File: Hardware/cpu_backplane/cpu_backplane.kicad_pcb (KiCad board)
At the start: 2 copper layers, 149.9 x 99.9 mm, 93 parts, among them J1 USB_B_Micro, J2 Conn_02x02_Odd_Even, J3 Conn_01x06, SW1 SW_SPST, U1 74AC161, U2 MAX811SEUS-T, U3 MAX811SEUS-T, U4 PAL24, U5 GAL16V8, U6 W65C02SxP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

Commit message: Fix missing signals
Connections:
- U5 pad 14: Net-(U5-Pad14) -> ~SIRQ~
- U9 pad 26: Net-(U9-Pad26) -> ~SIRQ~
- U9 pad 27: Net-(U9-Pad27) -> CLK
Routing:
- net ~SIRQ~: track 0.00 -> 63.2 mm, vias 0 -> 3
- net CLK: track 227.7 -> 268.8 mm, vias 7 -> 8
- net R~W~: track 268.9 -> 272.9 mm
- net /~DSR~: track 40.0 -> 44.0 mm

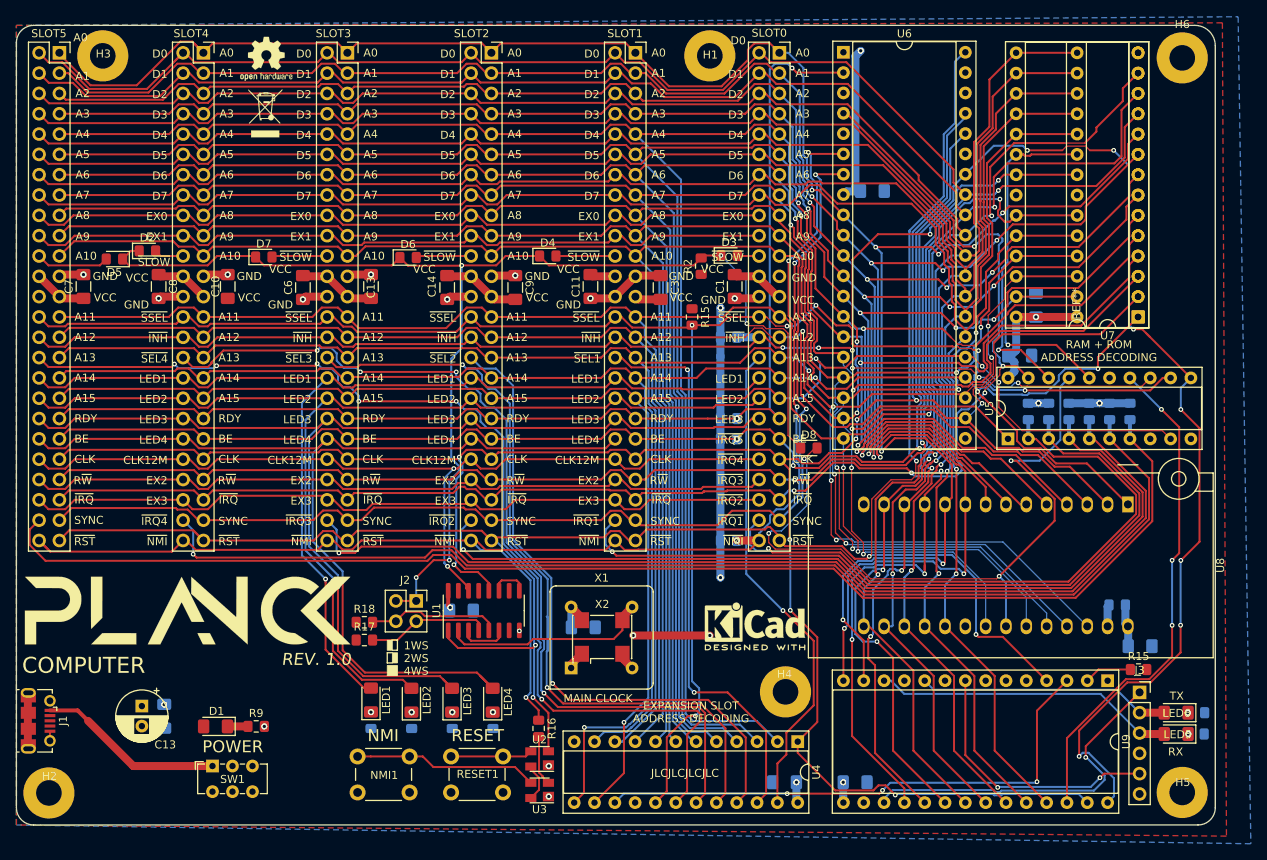
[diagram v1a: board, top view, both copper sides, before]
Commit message: Finishing CPU backplane with through hole components
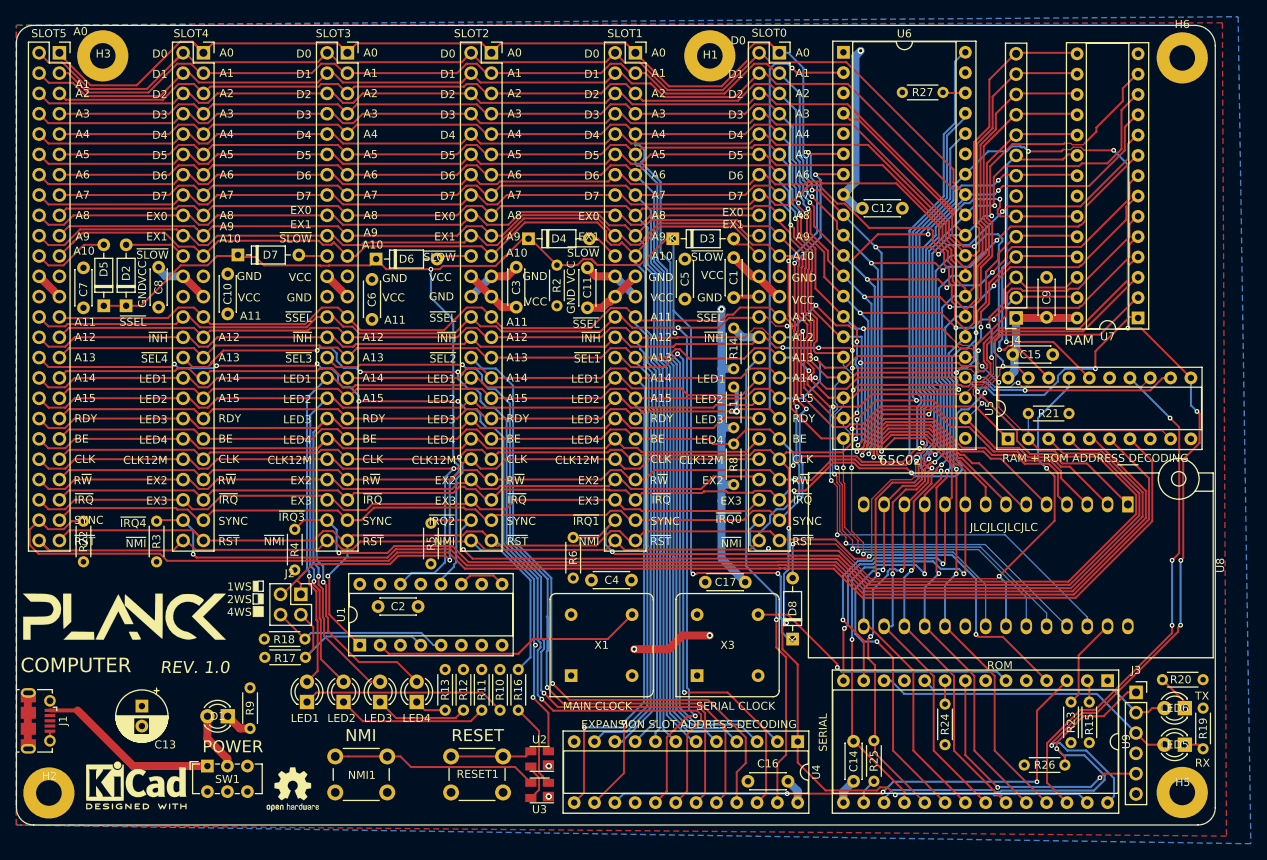
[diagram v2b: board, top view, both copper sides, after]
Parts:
- removed the C13 at (44.3, 32.6)
- removed the C14 at (53.8, 32.8)
- removed the C5 at (140.5, 77.6)
- removed the C5 at (55.6, 73.2)
- removed the C9 at (62.4, 32.8)
- removed the G*** at (21.4, 73.2)
- removed the G*** at (21.6, 73.7)
- removed H4: MountingHole_Pad, MountingHole:MountingHole_3.2mm_M3_Pad
- removed the R15 at (140.3, 80.5)
- removed the R15 at (84.5, 36.4)
- removed R7: 1k, Resistor_SMD:R_0805_2012Metric_Pad1.15x1.40mm_HandSolder
- removed the REF** at (140.2, 36.4)
- removed the REF** at (31.1, 11.0)
- removed X2: SG-7050CAN, Oscillator:Oscillator_SMD_SeikoEpson_SG8002CA-4Pin_7.0x5.0mm
- added C17: 10n, Capacitor_THT:C_Disc_D4.3mm_W1.9mm_P5.00mm, F.Cu at (86.1, 69.6)
- added C5: 10n, Capacitor_THT:C_Disc_D4.3mm_W1.9mm_P5.00mm, F.Cu at (83.6, 29.2)
- added G***: LOGO, Logo:logo-sm, B.Cu at (14.7, 74.4)
- added G***: LOGO, Logo:logo-sm, F.Cu at (13.5, 73.9)
- added J4: Conn_01x14, Connector_PinSocket_2.54mm:PinSocket_1x14_P2.54mm_Vertical, F.Cu at (125.0, 36.6)
- added R15: 10k, Resistor_THT:R_Axial_DIN0204_L3.6mm_D1.6mm_P5.08mm_Horizontal, F.Cu at (134.1, 84.6)
- added R24: 10k, Resistor_THT:R_Axial_DIN0204_L3.6mm_D1.6mm_P5.08mm_Horizontal, F.Cu at (116.1, 89.9)
- added R25: 10k, Resistor_THT:R_Axial_DIN0204_L3.6mm_D1.6mm_P5.08mm_Horizontal, F.Cu at (107.2, 89.4)
- added R26: 10k, Resistor_THT:R_Axial_DIN0204_L3.6mm_D1.6mm_P5.08mm_Horizontal, F.Cu at (126.0, 92.5)
- added R27: 10k, Resistor_THT:R_Axial_DIN0204_L3.6mm_D1.6mm_P5.08mm_Horizontal, F.Cu at (110.7, 8.38)
- added X3: 1.8432MHz, Oscillator:Oscillator_DIP-8, F.Cu at (85.1, 81.3)
- C1, C10, C11, C3, C6, C7, C8: footprint Capacitor_SMD:C_1206_3216Metric_Pad1.42x1.75mm_HandSolder -> Capacitor_THT:C_Disc_D4.3mm_W1.9mm_P5.00mm
- C12, C14, C15, C16, C2, C4, C9: footprint Capacitor_SMD:C_1206_3216Metric_Pad1.42x1.75mm_HandSolder -> Capacitor_THT:C_Disc_D4.3mm_W1.9mm_P5.00mm; moved to F.Cu
- D1, LED1, LED2, LED3, LED4, LED5, LED6: footprint LED_SMD:LED_1206_3216Metric_Pad1.42x1.75mm_HandSolder -> LED_THT:LED_D3.0mm
- D2, D3, D4, D5, D6, D7, D8: footprint Diode_SMD:D_0805_2012Metric_Pad1.15x1.40mm_HandSolder -> Diode_THT:D_DO-35_SOD27_P7.62mm_Horizontal
- R1, R10, R11, R12, R13, R14, R19, R20, R21, R22, R23, R3, R4, R5, R6, R8: footprint Resistor_SMD:R_0805_2012Metric_Pad1.15x1.40mm_HandSolder -> Resistor_THT:R_Axial_DIN0204_L3.6mm_D1.6mm_P5.08mm_Horizontal; moved to F.Cu
- R16, R17, R18, R2, R9: footprint Resistor_SMD:R_0805_2012Metric_Pad1.15x1.40mm_HandSolder -> Resistor_THT:R_Axial_DIN0204_L3.6mm_D1.6mm_P5.08mm_Horizontal
- U1: footprint Package_SO:SOIC-16_3.9x9.9mm_P1.27mm -> Package_DIP:DIP-16_W7.62mm_Socket
- moved R22 132.2 mm to (8.38, 67.1), turned to 90 degrees
- moved R3 120.6 mm to (17.5, 67.1), turned to 90 degrees
- moved R4 101.3 mm to (34.8, 68.1), turned to 90 degrees
- moved REF** 91.4 mm to (34.5, 95.5)
- moved R5 82.0 mm to (51.8, 67.3), turned to 90 degrees
- moved REF** 79.9 mm to (15.0, 95.0)
- moved R6 63.0 mm to (69.6, 69.1), turned to 90 degrees
- moved C2 30.0 mm to (45.2, 72.6), turned to 0 degrees
- moved D8 24.0 mm to (97.0, 76.7), turned to 90 degrees
- moved R2 18.7 mm to (67.6, 35.1)
- moved C3 18.2 mm to (62.5, 30.2)
- moved R23 18.2 mm to (131.8, 89.7), turned to 90 degrees
- moved R10 16.2 mm to (60.5, 85.6), turned to 90 degrees
- moved U1 16.1 mm to (42.9, 77.5)
- moved J2 14.4 mm to (35.6, 71.1)
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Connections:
- SLOT0 pad 40: LDE4 -> LED4
- U9 pad 16: GND -> Net-(R25-Pad2)
- U9 pad 9: GND -> /~CTS~
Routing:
- net ~SLOW~: track 160.1 -> 211.4 mm
- net Net-(U9-Pad6): track 0.00 -> 34.7 mm, vias 0 -> 1
- net Net-(LED1-Pad1): track 0.00 -> 25.5 mm, vias 1 -> 0
- net +5V: track 157.7 -> 134.5 mm, vias 10 -> 2
- net ~ROM_CS~: track 88.5 -> 69.2 mm, vias 4 -> 3
- net Net-(LED2-Pad1): track 0.00 -> 18.8 mm, vias 1 -> 0
- net GND: track 54.5 -> 37.4 mm, vias 16 -> 4
- net Net-(LED3-Pad1): track 0.00 -> 11.6 mm, vias 1 -> 0
- net LED3: track 144.1 -> 132.8 mm
- net ~NMI~: track 185.6 -> 176.1 mm, vias 5 -> 3
- net /~DSR~: track 44.0 -> 53.3 mm
- net Net-(R23-Pad2): track 2.74 -> 11.4 mm
- net LED2: track 141.2 -> 132.9 mm
- net /CLK_24M: track 25.9 -> 34.0 mm
- net A10: track 279.8 -> 286.8 mm
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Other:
- rule pad_to_mask_clearance: 0.05 -> 0
- board text added: "65C02"
- board text added: "RAM"
- board text added: "ROM"
- board text added: "SERIAL"
- board text added: "SERIAL CLOCK"
- board text added: "https://planck6502.com"
- board text added: "~IRQ0~"
- board text added: "©Jonathan Foucher 2021"
- board text removed: "~IRQ5~"

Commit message: update schematic and gerbers
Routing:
- net A8: track 283.5 -> 284.5 mm
- net ~RESET~: track 257.5 -> 258.1 mm

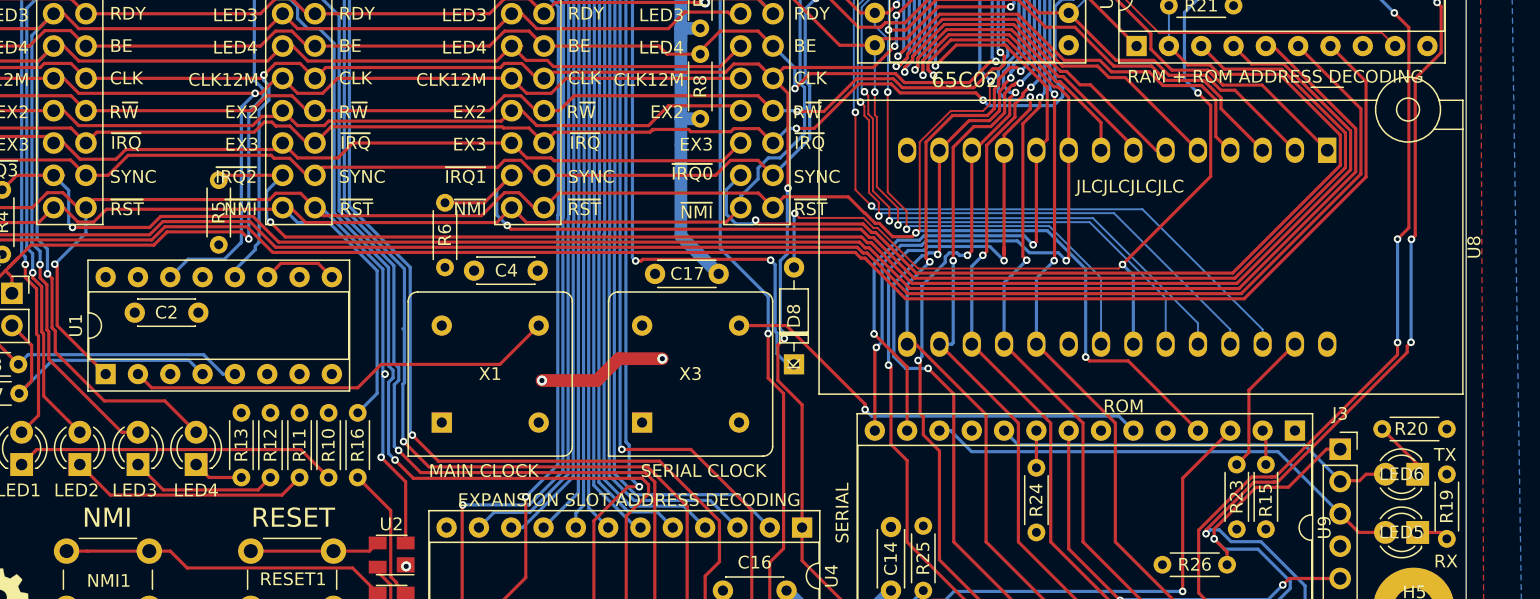
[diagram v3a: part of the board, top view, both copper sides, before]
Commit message: Use regular DIP socket
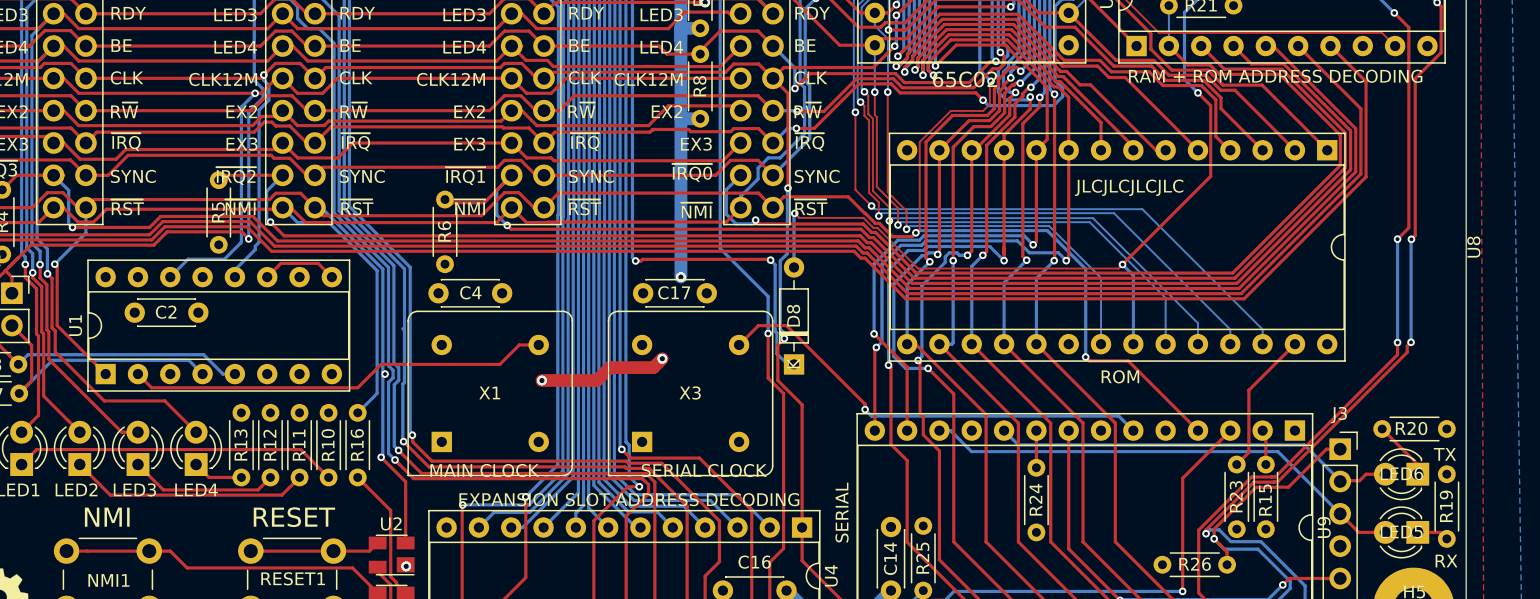
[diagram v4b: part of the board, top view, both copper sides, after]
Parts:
- U8: footprint Socket:DIP_Socket-28_W11.9_W12.7_W15.24_W17.78_W18.5_3M_228-1277-00-0602J -> Package_DIP:DIP-28_W15.24mm_Socket
- moved C17 4.34 mm to (90.2, 71.1), turned to 180 degrees
- moved C4 3.31 mm to (69.1, 71.1)
- moved X1 1.52 mm to (69.3, 82.8)
- moved X3 1.52 mm to (85.1, 82.8)
- moved R6 0.25 mm to (69.6, 68.8)
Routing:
- net +5V: track 134.5 -> 133.5 mm, vias 2 -> 3
- net Net-(U9-Pad6): track 34.7 -> 35.3 mm
- net /CLK_24M: track 34.0 -> 33.3 mm

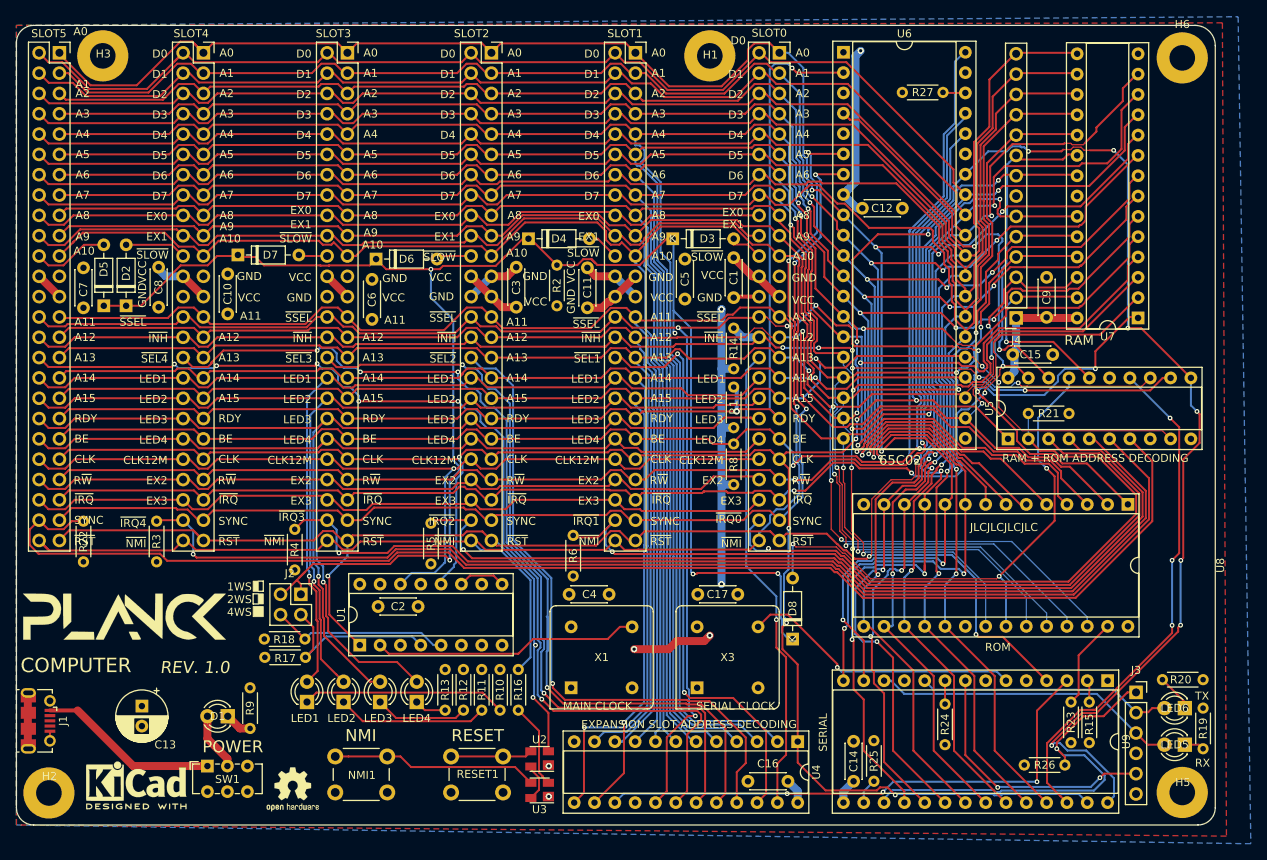
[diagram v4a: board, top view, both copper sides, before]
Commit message: replace resistors with bigger ones + fix diodes
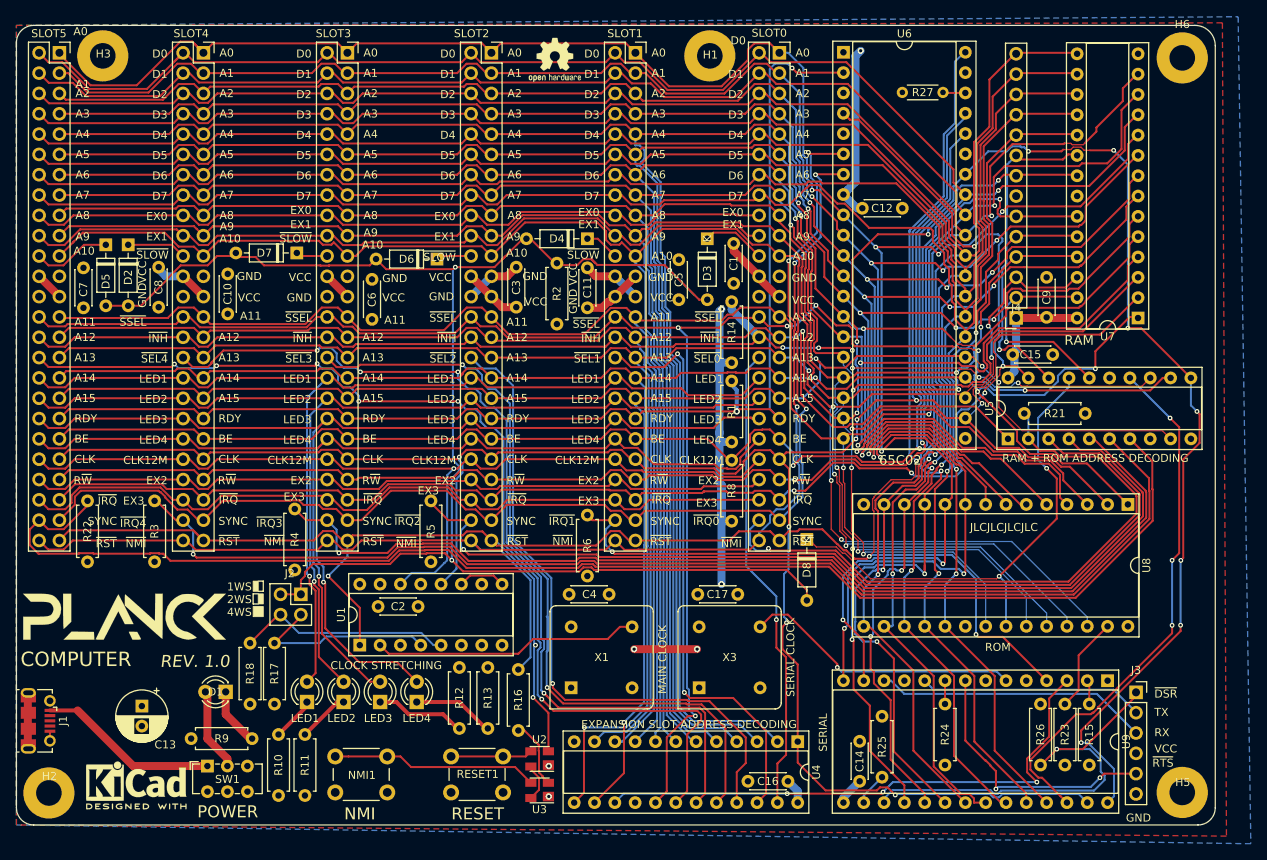
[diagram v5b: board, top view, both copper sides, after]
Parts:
- removed LED5, LED6: LED, LED_THT:LED_D3.0mm
- removed R19, R20: 470R, Resistor_THT:R_Axial_DIN0204_L3.6mm_D1.6mm_P5.08mm_Horizontal
- C7: value 47n -> 1u
- R1, R8: value 4.7k -> 10k; footprint Resistor_THT:R_Axial_DIN0204_L3.6mm_D1.6mm_P5.08mm_Horizontal -> Resistor_THT:R_Axial_DIN0207_L6.3mm_D2.5mm_P7.62mm_Horizontal
- R10, R11, R12, R13, R14, R15, R16, R17, R18, R2, R21, R22, R23, R24, R25, R26, R3, R4, R5, R6, R9: footprint Resistor_THT:R_Axial_DIN0204_L3.6mm_D1.6mm_P5.08mm_Horizontal -> Resistor_THT:R_Axial_DIN0207_L6.3mm_D2.5mm_P7.62mm_Horizontal
- moved REF** 96.9 mm to (67.3, 4.32)
- moved R10 27.9 mm to (32.8, 88.6), turned to 270 degrees
- moved R11 22.3 mm to (36.1, 88.6), turned to 270 degrees
- moved D8 12.6 mm to (98.8, 64.3), turned to 270 degrees
- moved R18 8.32 mm to (29.2, 84.8), turned to 90 degrees
- moved R26 7.89 mm to (128.0, 84.8), turned to 270 degrees
- moved D2 7.62 mm to (14.0, 27.4), turned to 270 degrees
- moved D5 7.62 mm to (11.2, 27.4), turned to 270 degrees
- moved D6 7.62 mm to (52.6, 29.2), turned to 180 degrees
- moved D7 7.37 mm to (35.1, 28.4), turned to 180 degrees
- moved D4 7.37 mm to (71.4, 26.7), turned to 180 degrees
- moved R17 5.97 mm to (32.3, 84.8), turned to 90 degrees
- moved R13 5.80 mm to (58.9, 87.9)
- moved C5 5.14 mm to (82.8, 34.3), turned to 90 degrees
- moved R8 4.58 mm to (89.4, 62.0)
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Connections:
- net RX renamed /RX
- net TX renamed /TX
- D2 pad 1: ~SLOW~ -> Net-(D2-Pad1)
- D2 pad 2: Net-(D2-Pad2) -> ~SLOW~
- D3 pad 1: ~SLOW~ -> Net-(D3-Pad1)
- D3 pad 2: Net-(D3-Pad2) -> ~SLOW~
- D4 pad 1: ~SLOW~ -> Net-(D4-Pad1)
- D4 pad 2: Net-(D4-Pad2) -> ~SLOW~
- D5 pad 1: ~SLOW~ -> Net-(D5-Pad1)
- D5 pad 2: Net-(D5-Pad2) -> ~SLOW~
- D6 pad 1: ~SLOW~ -> Net-(D6-Pad1)
- D6 pad 2: Net-(D6-Pad2) -> ~SLOW~
- D7 pad 1: ~SLOW~ -> Net-(D7-Pad1)
- D7 pad 2: Net-(D7-Pad2) -> ~SLOW~
- D8 pad 1: ~SLOW~ -> ~ROM_CS~
- D8 pad 2: ~ROM_CS~ -> ~SLOW~
- SLOT0 pad 22: Net-(D3-Pad2) -> Net-(D3-Pad1)
- SLOT1 pad 22: Net-(D4-Pad2) -> Net-(D4-Pad1)
- SLOT2 pad 22: Net-(D6-Pad2) -> Net-(D6-Pad1)
- SLOT3 pad 22: Net-(D7-Pad2) -> Net-(D7-Pad1)
- SLOT4 pad 22: Net-(D2-Pad2) -> Net-(D2-Pad1)
- SLOT5 pad 22: Net-(D5-Pad2) -> Net-(D5-Pad1)
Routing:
- net Net-(LED1-Pad1): track 25.5 -> 5.54 mm
- net Net-(LED2-Pad1): track 18.8 -> 6.51 mm
- net +5V: track 133.5 -> 143.4 mm
- net ~SLOW~: track 211.4 -> 201.5 mm, vias 5 -> 3
- net Net-(D5-Pad2): track 9.64 -> 0.00 mm
- net Net-(D5-Pad1): track 0.00 -> 9.64 mm
- net Net-(D2-Pad2): track 8.06 -> 0.00 mm
- net Net-(D2-Pad1): track 0.00 -> 8.06 mm
- net Net-(D3-Pad1): track 0.00 -> 8.00 mm
- net Net-(LED4-Pad1): track 3.98 -> 10.4 mm
- net ~ROM_CS~: track 69.2 -> 63.3 mm, vias 3 -> 2
- net SYNC: track 146.2 -> 152.0 mm
- net R~W~: track 275.1 -> 269.6 mm
- net GND: track 37.4 -> 31.9 mm
- net /DS2: track 22.3 -> 27.4 mm
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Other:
- board text added: "CLOCK STRETCHING"
- board text added: "~DSR~"
- board text added: "~RTS~"
- board text added: "~SEL0~"
